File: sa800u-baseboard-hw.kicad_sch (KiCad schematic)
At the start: 8 parts

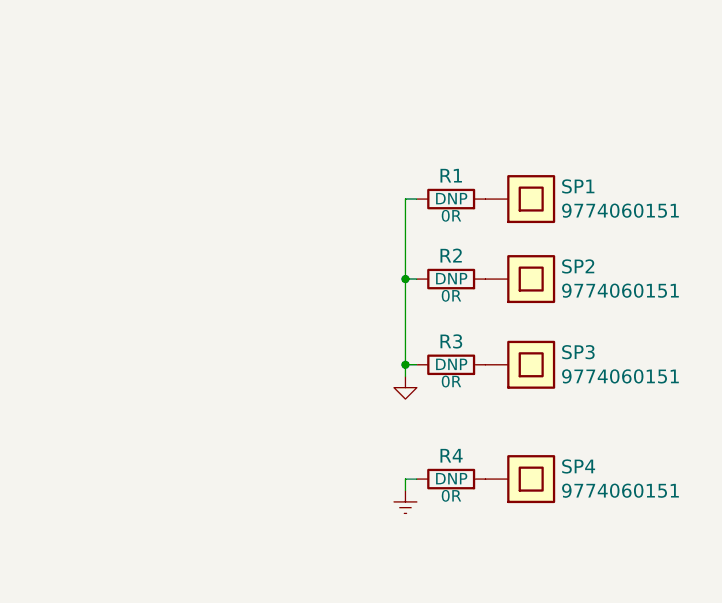
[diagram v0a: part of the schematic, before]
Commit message: Introduce component standardization
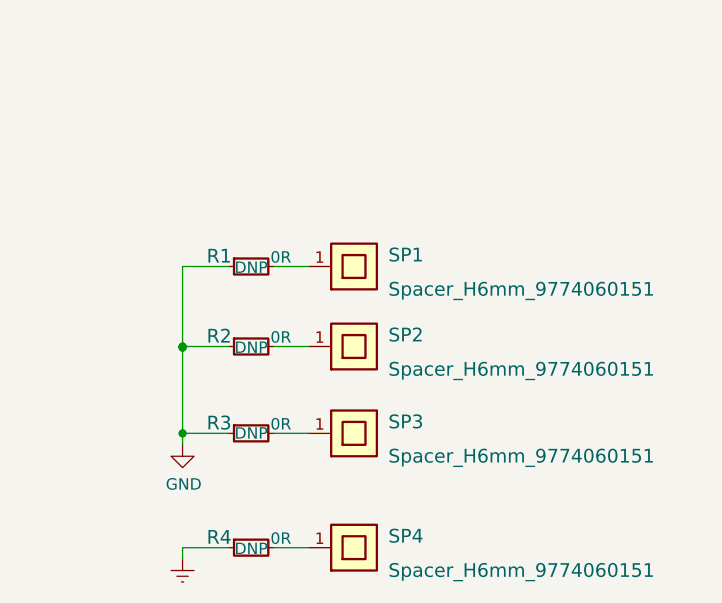
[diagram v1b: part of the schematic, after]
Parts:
- R1, R2, R3, R4: footprint sa800u-baseboard-hw-footprints:0402-res -> sa800u-baseboard-hw-footprints:R_0402_1005Metric; Author (none) -> Antmicro; Current (none) -> 1A; License (none) -> Apache-2.0; Manufacturer PANASONIC -> Panasonic
- SP1, SP2, SP3, SP4: value 9774060151 -> Spacer_H6mm_9774060151; footprint sa800u-baseboard-hw-footprints:9774060151 -> sa800u-baseboard-hw-footprints:Spacer_SMD_M2.5_H6mm_Wurth_9774060151; symbol sa800u-baseboard-hw:9774060151 -> sa800u-baseboard-hw:Spacer_H6mm_9774060151; Author (none) -> Antmicro; License (none) -> Apache-2.0; Manufacturer Wurth Elektronik -> Würth Elektronik
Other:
- moved on the sheet: R1, R2, R3, R4

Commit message: Add OHP assets
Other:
- company: (none) -> Antmicro Ltd.
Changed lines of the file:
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@@
   (title_block
     (title "SA800U (Snapdragon 845) Baseboard")
-    (date "2023-07-27")
-    (rev "1.0.2")
+    (date "2023-10-19")
+    (rev "1.0.3")
+    (company "Antmicro Ltd.")
     (comment 1 "www.antmicro.com")
-    (comment 2 "Antmicro Ltd.")
   )
   (junction (at 349.25 213.995) (diameter 0) (color 0 0 0 0)
@@
     )
   )
-  (symbol (lib_id "sa800u-baseboard-hw:Spacer_H6mm_9774060151") (at 363.22 223.52 0) (unit 1)
+  (symbol (lib_name "Spacer_H6mm_9774060151_1") (lib_id "sa800u-baseboard-hw:Spacer_H6mm_9774060151") (at 363.22 223.52 0) (unit 1)
     (in_bom yes) (on_board yes) (fields_autoplaced)
     (property "Reference" "SP3" (id 0) (at 372.11 222.25 0)
@@
     (pin "1")
   )
-  (symbol (lib_id "sa800u-baseboard-hw:Spacer_H6mm_9774060151") (at 363.22 236.22 0) (unit 1)
+  (symbol (lib_name "Spacer_H6mm_9774060151_3") (lib_id "sa800u-baseboard-hw:Spacer_H6mm_9774060151") (at 363.22 236.22 0) (unit 1)
     (in_bom yes) (on_board yes) (fields_autoplaced)
     (property "Reference" "SP4" (id 0) (at 372.11 234.95 0)
@@
     (pin "1")
   )
-  (symbol (lib_id "sa800u-baseboard-hw:Spacer_H6mm_9774060151") (at 363.22 204.978 0) (unit 1)
+  (symbol (lib_name "Spacer_H6mm_9774060151_2") (lib_id "sa800u-baseboard-hw:Spacer_H6mm_9774060151") (at 363.22 204.978 0) (unit 1)
     (in_bom yes) (on_board yes) (fields_autoplaced)
     (property "Reference" "SP1" (id 0) (at 372.11 203.708 0)
@@
       (reference "#FLG027") (unit 1) (value "PWR_FLAG") (footprint "")
     )
+    (path "/00000000-0000-0000-0000-0000618e716e/8536f096-f72e-4eeb-9ced-e624df8aa944"
+      (reference "#FLG028") (unit 1) (value "PWR_FLAG") (footprint "")
+    )
+    (path "/00000000-0000-0000-0000-000061a19323/d16dfe71-1286-44fa-8a9e-dae916cf88b6"
+      (reference "#FLG0101") (unit 1) (value "PWR_FLAG") (footprint "")
+    )
+    (path "/00000000-0000-0000-0000-000061a19323/2f937ec4-fc38-4f40-b261-79c4d68f90e5"
+      (reference "#FLG0102") (unit 1) (value "PWR_FLAG") (footprint "")
+    )
+    (path "/00000000-0000-0000-0000-000061a19323/5962f944-d040-453b-848e-c6c81591d0b5"
+      (reference "#FLG0103") (unit 1) (value "PWR_FLAG") (footprint "")
+    )
+    (path "/00000000-0000-0000-0000-000061a60486/3bb31c40-ea2b-4c85-b1ce-6ede1f92aa82"
+      (reference "#FLG0104") (unit 1) (value "PWR_FLAG") (footprint "")
+    )
+    (path "/00000000-0000-0000-0000-00006197686d/95e6ad5b-addf-47ba-ba5e-479da1cb1e34"
+      (reference "#FLG0105") (unit 1) (value "PWR_FLAG") (footprint "")
+    )
+    (path "/00000000-0000-0000-0000-000061df77ce/63127df5-f6ec-4384-993d-48aba2bc254e"
+      (reference "#FLG0106") (unit 1) (value "PWR_FLAG") (footprint "")
+    )
+    (path "/00000000-0000-0000-0000-000061c01d88/ea63a2c2-c41d-456d-aee8-c267d660bc36"
+      (reference "#FLG0107") (unit 1) (value "PWR_FLAG") (footprint "")
+    )
+    (path "/00000000-0000-0000-0000-000061a2f307/7eb98e46-cd86-47de-92f4-5de884e5b561"
+      (reference "#FLG0108") (unit 1) (value "PWR_FLAG") (footprint "")
+    )
+    (path "/00000000-0000-0000-0000-000061a4bc4f/64d5374a-ef00-412a-bab1-91a9d24808bc"
+      (reference "#FLG0109") (unit 1) (value "PWR_FLAG") (footprint "")
+    )
     (path "/00000000-0000-0000-0000-000061fb7969"
       (reference "#PWR01") (unit 1) (value "GND") (footprint "")
@@
       (reference "#PWR0105") (unit 1) (value "GND") (footprint "")
     )
+    (path "/00000000-0000-0000-0000-000061a19323/a60bdf7d-0970-4d7a-b9ed-4b2c9e231bb5"
+      (reference "#PWR0106") (unit 1) (value "GNDD") (footprint "")
+    )
     (path "/00000000-0000-0000-0000-000061a4bc4f/00000000-0000-0000-0000-000061f5ab91"
       (reference "#PWR0141") (unit 1) (value "GND") (footprint "")
@@
       (reference "#PWR0271") (unit 1) (value "GND") (footprint "")
     )
+    (path "/00000000-0000-0000-0000-000061a4bc4f/e22e6b12-0038-4122-b24c-ba436784e1a0"
+      (reference "A1") (unit 1) (value "SA800U-WF") (footprint "sa800u-baseboard-hw-footprints:SA800U-WF")
+    )
     (path "/00000000-0000-0000-0000-000061a4bc4f/00000000-0000-0000-0000-000061b43805"
       (reference "BAT1") (unit 1) (value "Battery_Holder_MS621FE-FL11E") (footprint "sa800u-baseboard-hw-footprints:MS621FE-FL11E")
@@
       (reference "L29") (unit 1) (value "L_2u2_6.1A_XEL4030") (footprint "sa800u-baseboard-hw-footprints:L_Coilcraft_XEL4030")
     )
-    (path "/00000000-0000-0000-0000-000061a4bc4f/00000000-0000-0000-0000-000064251c32"
-      (reference "M1") (unit 1) (value "SA800U-WF-mechanical_model") (footprint "sa800u-baseboard-hw-footprints:SA800U-WF_mechanical_model")
-    )
     (path "/00000000-0000-0000-0000-000061b13669/00000000-0000-0000-0000-000061faa229"
       (reference "M2") (unit 1) (value "Mech_M2_2280_H4mm") (footprint "sa800u-baseboard-hw-footprints:Mech_M2_2280_H4mm")
@@
       (reference "U10") (unit 1) (value "NTS0102_XSON") (footprint "sa800u-baseboard-hw-footprints:XSON-8_1x1.95mm_P0.5mm")
     )
-    (path "/00000000-0000-0000-0000-000061a4bc4f/00000000-0000-0000-0000-000061b940c3"
-      (reference "U11") (unit 1) (value "SA800U-WF") (footprint "sa800u-baseboard-hw-footprints:SA800U-WF")
+    (path "/00000000-0000-0000-0000-000061a4bc4f/a1a83752-18a7-43af-8800-2d6b35b75313"
+      (reference "U11") (unit 1) (value "Receptacle_SA800U-WF") (footprint "sa800u-baseboard-hw-footprints:Receptacle_SA800U-WF")
     )
-    (path "/00000000-0000-0000-0000-000061a4bc4f/00000000-0000-0000-0000-000061baf70e"
-      (reference "U11") (unit 2) (value "SA800U-WF") (footprint "sa800u-baseboard-hw-footprints:SA800U-WF")
+    (path "/00000000-0000-0000-0000-000061a4bc4f/657d41a8-ce69-4bfc-bae1-7204f14b6e0c"
+      (reference "U11") (unit 2) (value "Receptacle_SA800U-WF") (footprint "sa800u-baseboard-hw-footprints:Receptacle_SA800U-WF")
     )
     (path "/00000000-0000-0000-0000-000061a60486/00000000-0000-0000-0000-000062338ad1"
